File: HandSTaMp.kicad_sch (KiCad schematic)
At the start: 25 parts, among them J1 USB_C_Receptacle_USB2.0_16P, J2 SWD, J3 Pins, J4 F2, SW0 BOOT, SW1 Row 0, Col+0, SW2 Row 0, Col+1, U1 STM32C071GBUx, U2 PRTR5V0U2X, U3 XC6206P332MR-G

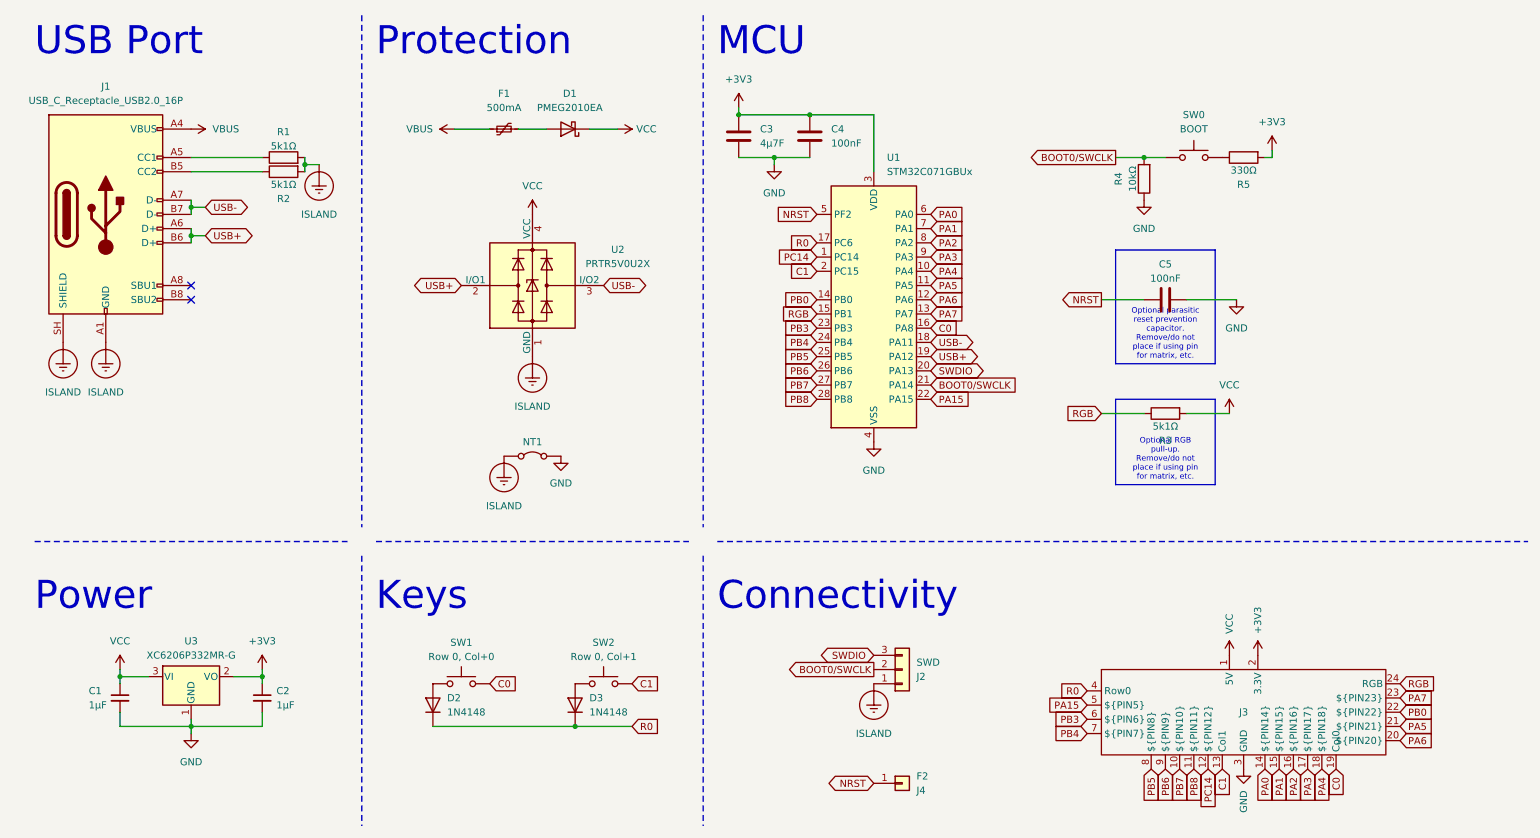
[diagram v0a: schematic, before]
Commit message: Draft of version using CH32X035G8U6
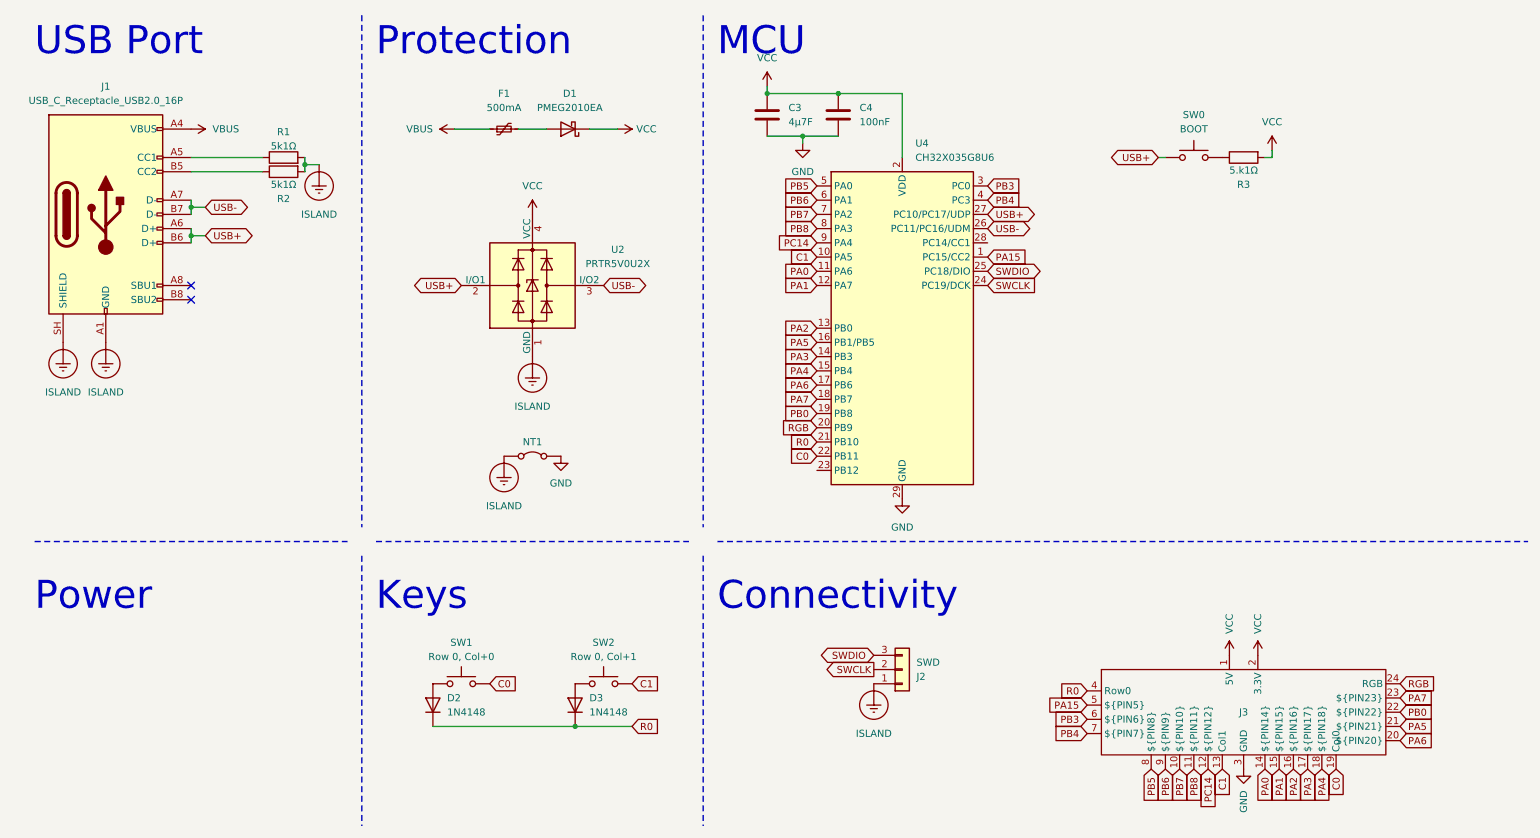
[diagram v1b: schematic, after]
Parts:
- removed C1, C2: 1µF, Capacitor_SMD:C_0603_1608Metric, symbol Device:C_Small
- removed C5: 100nF, Capacitor_SMD:C_0603_1608Metric, symbol Device:C
- removed J4: F2, TestPoint:TestPoint_THTPad_D1.0mm_Drill0.5mm, symbol Connector_Generic:Conn_01x01
- removed R3: 5k1Ω, Resistor_SMD:R_0603_1608Metric, symbol Device:R
- removed R4: 10kΩ, Resistor_SMD:R_0603_1608Metric, symbol Device:R
- removed U1: STM32C071GBUx, Package_DFN_QFN:QFN-28_4x4mm_P0.5mm, symbol MCU_ST_STM32C0:STM32C071GBUx
- removed U3: XC6206P332MR-G, Package_TO_SOT_SMD:SOT-23-3, symbol Regulator_Linear:XC6206PxxxMR
- added U4: CH32X035G8U6, Package_DFN_QFN:WQFN-28-1EP_4x4mm_P0.4mm_EP2.7x2.7mm, symbol MCU_WCH_RiscV:CH32X035G8U6
- R3: renamed from R5; value 330Ω -> 5.k1Ω
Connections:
- net +3V3 is gone; now on net VCC: C3.1, C4.1, J3.2 (3.3V), R3.2
- net C0: now also U4.22 (PB11)
- net C1: now also U4.10 (PA5)
- net GND: now also U4.29 (GND)
- net PA0: now also U4.11 (PA6)
- net PA1: now also U4.12 (PA7)
- net PA15: now also U4.1 (PC15/CC2)
- net PA2: now also U4.13 (PB0)
- net PA3: now also U4.14 (PB3)
- net PA4: now also U4.15 (PB4)
- net PA5: now also U4.16 (PB1/PB5)
- net PA6: now also U4.17 (PB6)
- net PA7: now also U4.18 (PB7)
- net PB0: now also U4.19 (PB8)
- net PB3: now also U4.3 (PC0)
- net PB4: now also U4.4 (PC3)
- net PB5: now also U4.5 (PA0)
- net PB6: now also U4.6 (PA1)
- net PB7: now also U4.7 (PA2)
- net PB8: now also U4.8 (PA3)
- net PC14: now also U4.9 (PA4)
- net R0: now also U4.21 (PB10)
- net RGB: now also U4.20 (PB9)
- net SWDIO: now also U4.25 (PC18/DIO)
- net USB+: now also SW0.1, U4.27 (PC10/PC17/UDP)
- net USB-: now also U4.26 (PC11/PC16/UDM)
- net VCC: now also U4.2 (VDD)
- net BOOT0/SWCLK renamed SWCLK
- net SWCLK: now also U4.24 (PC19/DCK); no longer SW0.1

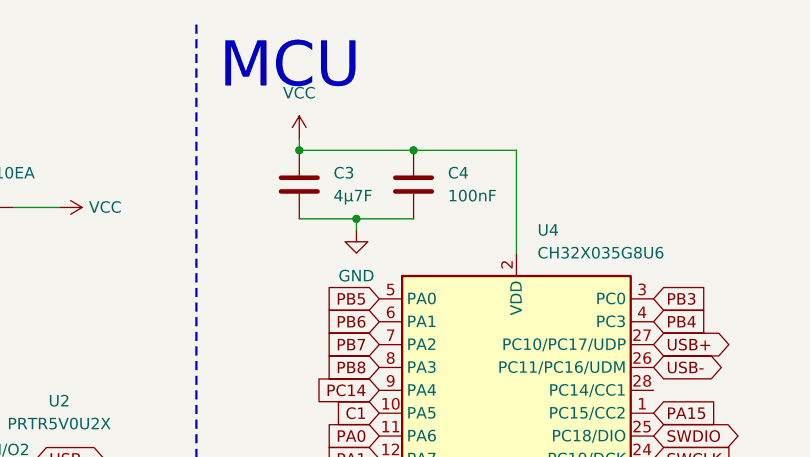
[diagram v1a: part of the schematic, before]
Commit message: Tweak routing and silkscreen, and update README
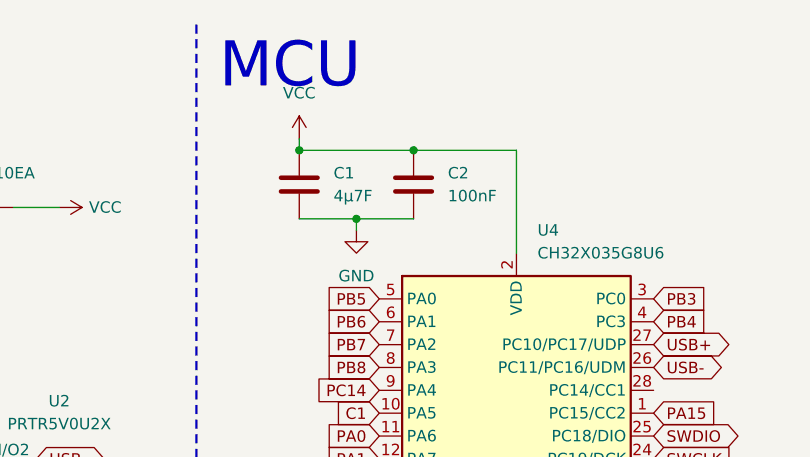
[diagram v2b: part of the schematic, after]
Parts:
- C1: renamed from C3; Label (none) -> µ
- C2: renamed from C4; Label (none) -> n
- F1: Label (none) -> F
- R3: Label (none) -> 3
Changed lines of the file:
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@@
 		(in_pos_files yes)
 		(dnp no)
-		(property "Reference" "C3"
+		(property "Reference" "C1"
 			(at 149.86 31.7499 0)
 			(show_name no)
@@
 		)
 		(property "MPN" "CL10A475KO8NNNC"
+			(at 146.05 33.02 0)
+			(hide yes)
+			(show_name no)
+			(do_not_autoplace no)
+			(effects
+				(font
+					(size 1.27 1.27)
+				)
+			)
+		)
+		(property "Label" "µ"
 			(at 146.05 33.02 0)
 			(hide yes)
@@
 			(project "HandSTaMp"
 				(path "/34400e51-cf83-464a-b3ec-e9a28a972a27"
-					(reference "C3")
+					(reference "C1")
 					(unit 1)
 				)
@@
 			)
 		)
+		(property "Label" "F"
+			(at 99.06 35.56 90)
+			(hide yes)
+			(show_name no)
+			(do_not_autoplace no)
+			(effects
+				(font
+					(size 1.27 1.27)
+				)
+			)
+		)
 		(pin "2"
 		)
@@
 		(dnp no)
 		(fields_autoplaced yes)
-		(property "Reference" "C4"
+		(property "Reference" "C2"
 			(at 162.56 31.75 0)
 			(show_name no)
@@
 		)
 		(property "MPN" "CL10B104KO8NNNC"
+			(at 158.75 33.02 0)
+			(hide yes)
+			(show_name no)
+			(do_not_autoplace no)
+			(effects
+				(font
+					(size 1.27 1.27)
+				)
+			)
+		)
+		(property "Label" "n"
 			(at 158.75 33.02 0)
 			(hide yes)
@@
 			(project "HandSTaMp"
 				(path "/34400e51-cf83-464a-b3ec-e9a28a972a27"
-					(reference "C4")
+					(reference "C2")
 					(unit 1)
 				)
@@
 			(at 231.14 40.64 90)
 			(hide yes)
+			(show_name no)
+			(do_not_autoplace no)
+			(effects
+				(font
+					(size 1.27 1.27)
+				)
+			)
+		)
+		(property "Label" "3"
+			(at 231.14 40.64 90)
+			(hide yes)

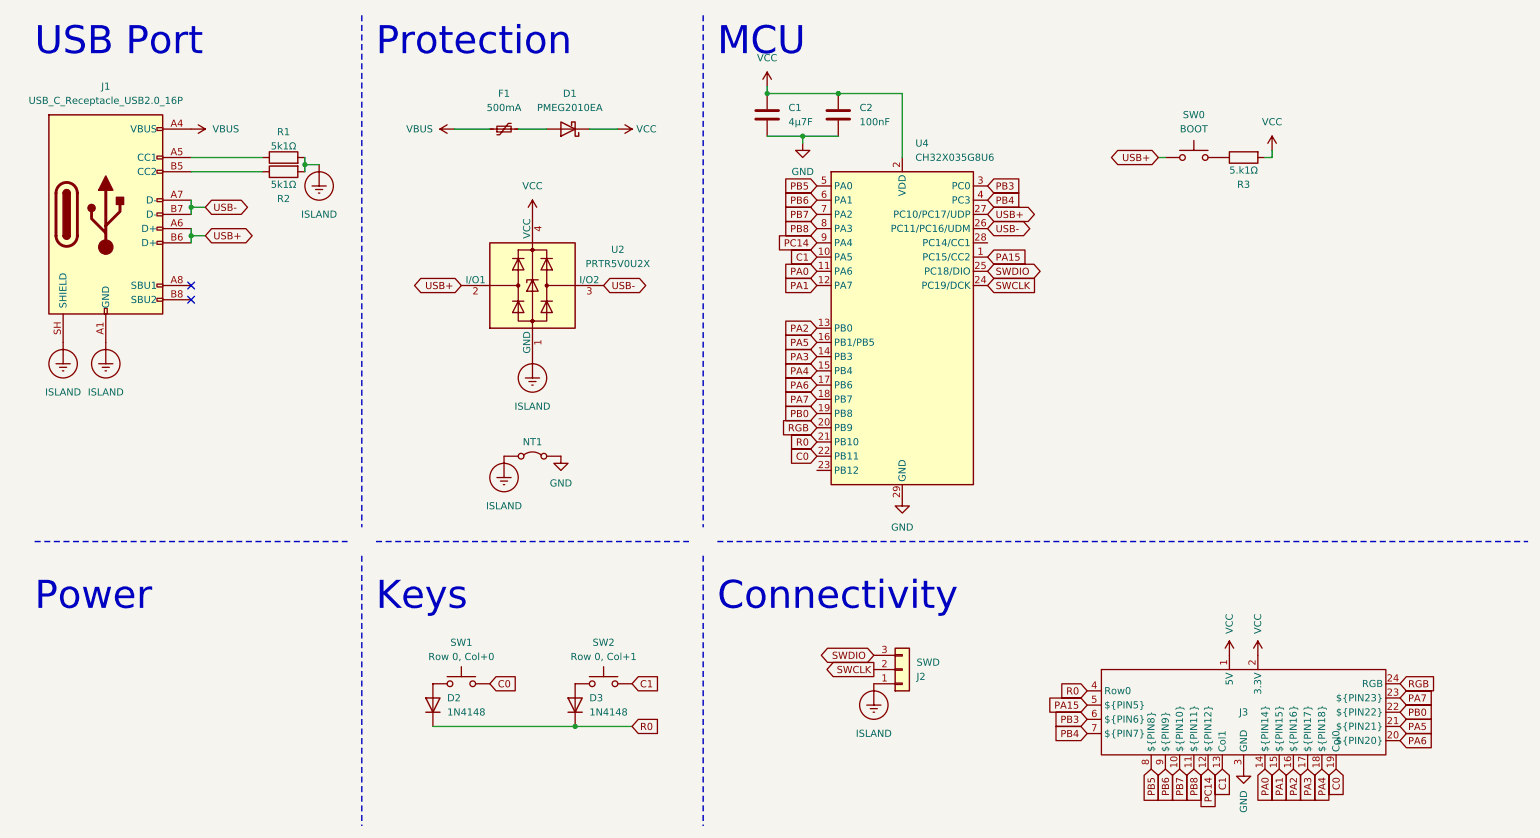
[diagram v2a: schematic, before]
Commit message: Update internal and external pin labelling
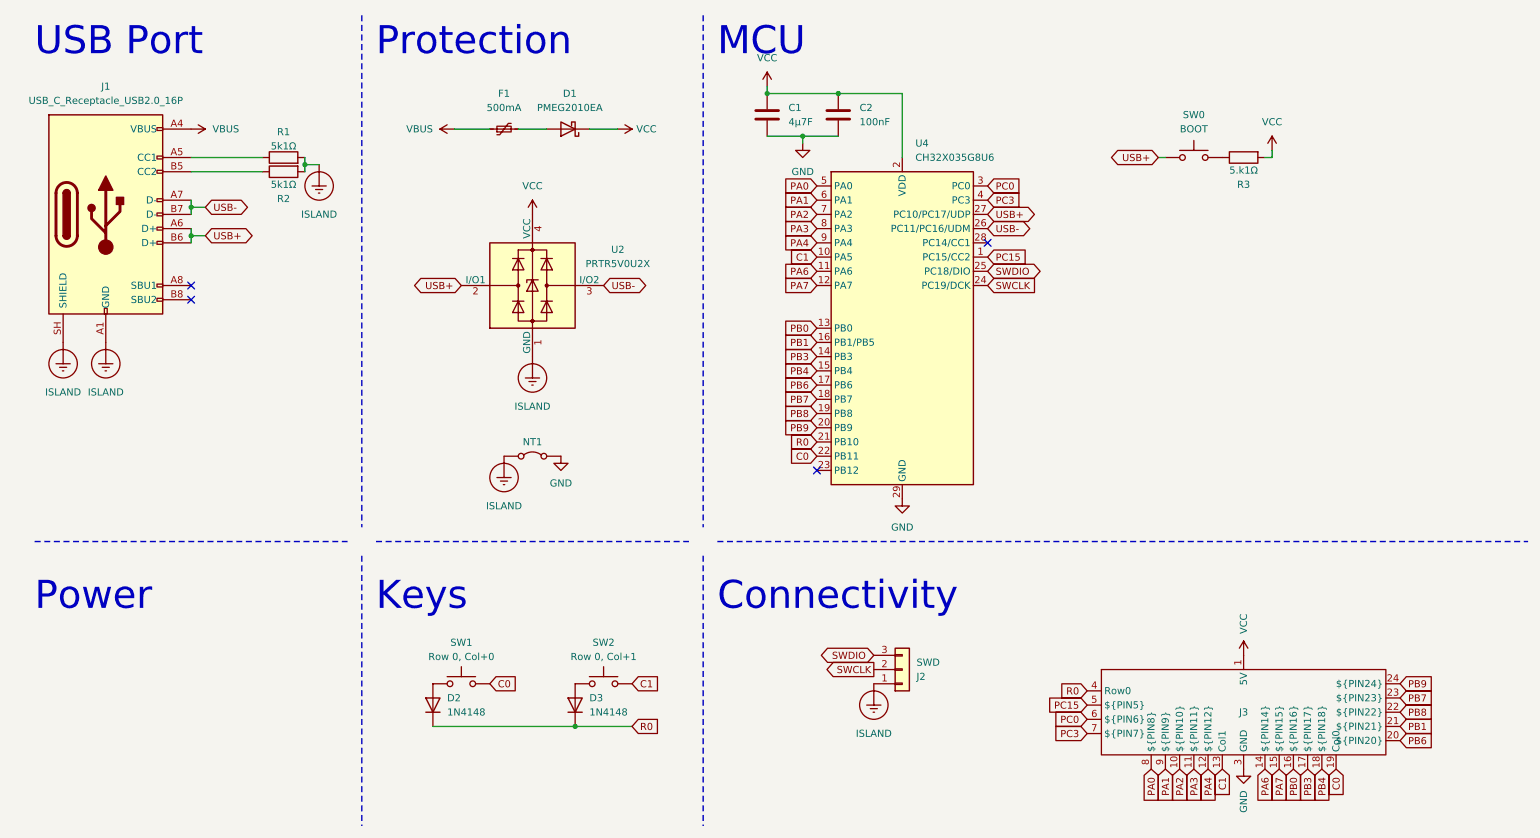
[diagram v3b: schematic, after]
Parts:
- J3: PIN10 B7 -> A2; PIN11 B8 -> A3; PIN12 C14 -> A4; PIN14 A0 -> A6; PIN15 A1 -> A7; PIN16 A2 -> B0; PIN17 A3 -> B3; PIN18 A4 -> B4; PIN20 A6 -> B6; PIN21 A5 -> B1; PIN22 B0 -> B8; PIN23 A7 -> B7; PIN24 (none) -> B9; PIN5 A15 -> C15; PIN6 B3 -> C0; PIN7 B4 -> C3; PIN8 B5 -> A0; PIN9 B6 -> A1
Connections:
- net PB5 is gone; now on net PA0: J3.8 (${PIN8}), U4.5 (PA0)
- net PC14 is gone; now on net PA4: J3.12 (${PIN12}), U4.9 (PA4)
- net PA0: no longer J3.14 (${PIN14}), U4.11 (PA6)
- net PA1: now also J3.9 (${PIN9}), U4.6 (PA1); no longer J3.15 (${PIN15}), U4.12 (PA7)
- net PA2: now also J3.10 (${PIN10}), U4.7 (PA2); no longer J3.16 (${PIN16}), U4.13 (PB0)
- net PA3: now also J3.11 (${PIN11}), U4.8 (PA3); no longer J3.17 (${PIN17}), U4.14 (PB3)
- net PA4: no longer J3.18 (${PIN18}), U4.15 (PB4)
- net PA6: now also J3.14 (${PIN14}), U4.11 (PA6); no longer J3.20 (${PIN20}), U4.17 (PB6)
- net PA7: now also J3.15 (${PIN15}), U4.12 (PA7); no longer J3.23 (${PIN23}), U4.18 (PB7)
- net PB0: now also J3.16 (${PIN16}), U4.13 (PB0); no longer J3.22 (${PIN22}), U4.19 (PB8)
- net PB3: now also J3.17 (${PIN17}), U4.14 (PB3); no longer J3.6 (${PIN6}), U4.3 (PC0)
- net PB4: now also J3.18 (${PIN18}), U4.15 (PB4); no longer J3.7 (${PIN7}), U4.4 (PC3)
- net PB6: now also J3.20 (${PIN20}), U4.17 (PB6); no longer J3.9 (${PIN9}), U4.6 (PA1)
- net PB7: now also J3.23 (${PIN23}), U4.18 (PB7); no longer J3.10 (${PIN10}), U4.7 (PA2)
- net PB8: now also J3.22 (${PIN22}), U4.19 (PB8); no longer J3.11 (${PIN11}), U4.8 (PA3)
- net VCC: no longer J3.2 (3.3V)
- net PA15 renamed PC15
- net PA5 renamed PB1
- net RGB renamed PB9
- new net PC0: J3.6 (${PIN6}), U4.3 (PC0)
- new net PC3: J3.7 (${PIN7}), U4.4 (PC3)
- no-connect marks 2 -> 4
